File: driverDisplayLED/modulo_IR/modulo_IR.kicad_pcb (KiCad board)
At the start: 2 copper layers, 15 parts, among them J1 Conn_01x03_Male, U1 SFH617A-1X001, U2 LM393

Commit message: rediseño PCB
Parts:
- removed U1: SFH617A-1X001, Package_SO:SO-4_4.4x2.3mm_P1.27mm
- added D3: LED, LED_THT:LED_D5.0mm_Horizontal_O3.81mm_Z3.0mm, F.Cu at (111.0, 77.0)
- added D4: D_Photo, LED_THT:LED_D5.0mm_Horizontal_O3.81mm_Z3.0mm, F.Cu at (111.0, 84.5)
- C1, C2: footprint Capacitor_SMD:C_0504_1310Metric_Pad0.83x1.28mm_HandSolder -> Capacitor_SMD:C_0805_2012Metric
- D1, D2: footprint LED_THT:LED_D1.8mm_W3.3mm_H2.4mm -> Diode_SMD:D_0805_2012Metric
- J1: footprint Connector_PinHeader_2.54mm:PinHeader_1x03_P2.54mm_Vertical -> Connector_PinHeader_2.54mm:PinHeader_1x03_P2.54mm_Horizontal
- moved D2 28.2 mm to (138.9, 76.0), turned to 0 degrees
- moved D1 28.1 mm to (139.1, 88.0), turned to 0 degrees
- moved H1 5.05 mm to (137.0, 80.0)
- moved J1 3.42 mm to (144.0, 80.0)
- moved H2 1.61 mm to (115.0, 77.0)
- moved U2 1.16 mm to (129.0, 86.6)
- moved C1 0.91 mm to (121.5, 76.2), turned to 180 degrees
- moved R3 0.82 mm to (135.0, 85.9), turned to 270 degrees
- moved RV1 0.80 mm to (129.0, 78.0)
- moved R1 0.65 mm to (121.3, 88.2), turned to 180 degrees
- moved C2 0.51 mm to (121.5, 78.8), turned to 180 degrees
- moved R4 0.36 mm to (121.3, 85.8)
- moved R2 0.31 mm to (121.3, 83.5)
- moved R5 0.25 mm to (121.4, 81.2)
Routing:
- net Net-(C2-Pad1): track 41.5 -> 19.9 mm, vias 3 -> 1
- net Net-(D3-Pad2): track 13.1 -> 32.8 mm, vias 0 -> 1
- net Net-(D2-Pad1): track 11.0 -> 30.1 mm, vias 0 -> 2
- net +5V: track 104.4 -> 91.8 mm, vias 0 -> 2
- net Net-(D1-Pad1): track 10.2 -> 17.2 mm
- net Net-(RV1-Pad2): track 11.5 -> 13.6 mm
- net (no net): track 0.98 -> 0.00 mm
- net GND: vias 2 -> 0
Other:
- board outline added: 40 x 18 mm
- rule trace_min: 0.2 -> 0.3
- rule via_min_size: 0.4 -> 0.5

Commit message: rediseño PCB
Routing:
- net +5V: track 91.8 -> 93.6 mm
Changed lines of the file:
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@@
     (thickness 1.6)
     (drawings 5)
-    (tracks 95)
+    (tracks 97)
     (zones 0)
     (modules 16)
@@
   (segment (start 123.75 76.25) (end 122.5 76.25) (width 0.3) (layer F.Cu) (net 1))
   (segment (start 140 88) (end 140 87) (width 0.3) (layer F.Cu) (net 1))
-  (segment (start 138 85) (end 136 85) (width 0.3) (layer F.Cu) (net 1))
   (segment (start 140 87) (end 138 85) (width 0.3) (layer F.Cu) (net 1))
   (via (at 125 76) (size 1) (drill 0.5) (layers F.Cu B.Cu) (net 1))
@@
   (segment (start 114 82) (end 115 81) (width 0.3) (layer F.Cu) (net 1))
   (segment (start 114 84) (end 114 82) (width 0.3) (layer F.Cu) (net 1))
+  (segment (start 136.75 85) (end 135 85) (width 0.3) (layer F.Cu) (net 1))
+  (segment (start 138 85) (end 136.75 85) (width 0.3) (layer F.Cu) (net 1))
+  (segment (start 136.75 85) (end 136 85) (width 0.3) (layer F.Cu) (net 1))
   (segment (start 126.525 87.23) (end 125.23 87.23) (width 0.3) (layer F.Cu) (net 3))
   (segment (start 123.75 85.75) (end 122.25 85.75) (width 0.3) (layer F.Cu) (net 3))

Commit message: actualizo correcciones PCB, con DRC sin errores, margenes actualizdos, mounting hole y fiducial, labels, y planos de Vcc y GND
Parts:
- H2: footprint Fiducial:Fiducial_1mm_Mask2mm -> MountingHole:MountingHole_2.2mm_M2
- moved H1 22.5 mm to (115.0, 75.2)
- moved H2 21.2 mm to (136.0, 79.6)
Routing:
- net +5V: track 93.6 -> 37.6 mm, vias 2 -> 0
- net Net-(C2-Pad1): track 19.9 -> 28.1 mm, vias 1 -> 2
- net GND: track 0.00 -> 8.14 mm, vias 0 -> 2
- net Net-(D3-Pad2): track 32.8 -> 35.6 mm
- added copper zone on F.Cu, net +5V
- removed copper zone on F.Cu, net GND
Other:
- net class Default: trace_width 0.25 -> 0.3; via_dia 0.8 -> 1; via_drill 0.4 -> 0.5

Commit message: actualizo rotulo
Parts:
- moved C1 43.2 mm to (81.0, 91.2)
- moved C2 43.2 mm to (81.0, 93.8)
- moved D1 43.2 mm to (98.6, 103.0)
- moved D2 43.2 mm to (98.4, 91.0)
- moved D3 43.2 mm to (70.5, 92.0)
- moved D4 43.2 mm to (70.5, 99.5)
- moved H1 43.2 mm to (74.5, 90.2)
- moved H2 43.2 mm to (95.5, 94.6)
- moved J1 43.2 mm to (103.5, 95.0)
- moved R1 43.2 mm to (80.8, 103.2)
- moved R2 43.2 mm to (80.8, 98.5)
- moved R3 43.2 mm to (94.5, 100.9)
- moved R4 43.2 mm to (80.8, 100.8)
- moved R5 43.2 mm to (80.9, 96.2)
- moved RV1 43.2 mm to (88.5, 93.0)
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
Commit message: agrego notas de fabricacion
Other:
- board text added: "Estandar 8 mils (ref. Mayer) Grilla: 1 mm, 0.5 mm Via: 0.8 mm / 0.4 mm Margen: 0.4 mm Pista: 0.3 mm Dist a Borde: 0.5 mm Terminacion : Cu+Flux Espesor placa: 1.6 mm Espesor del Cobre: Estandar (35um/1Oz) Material: FR4"

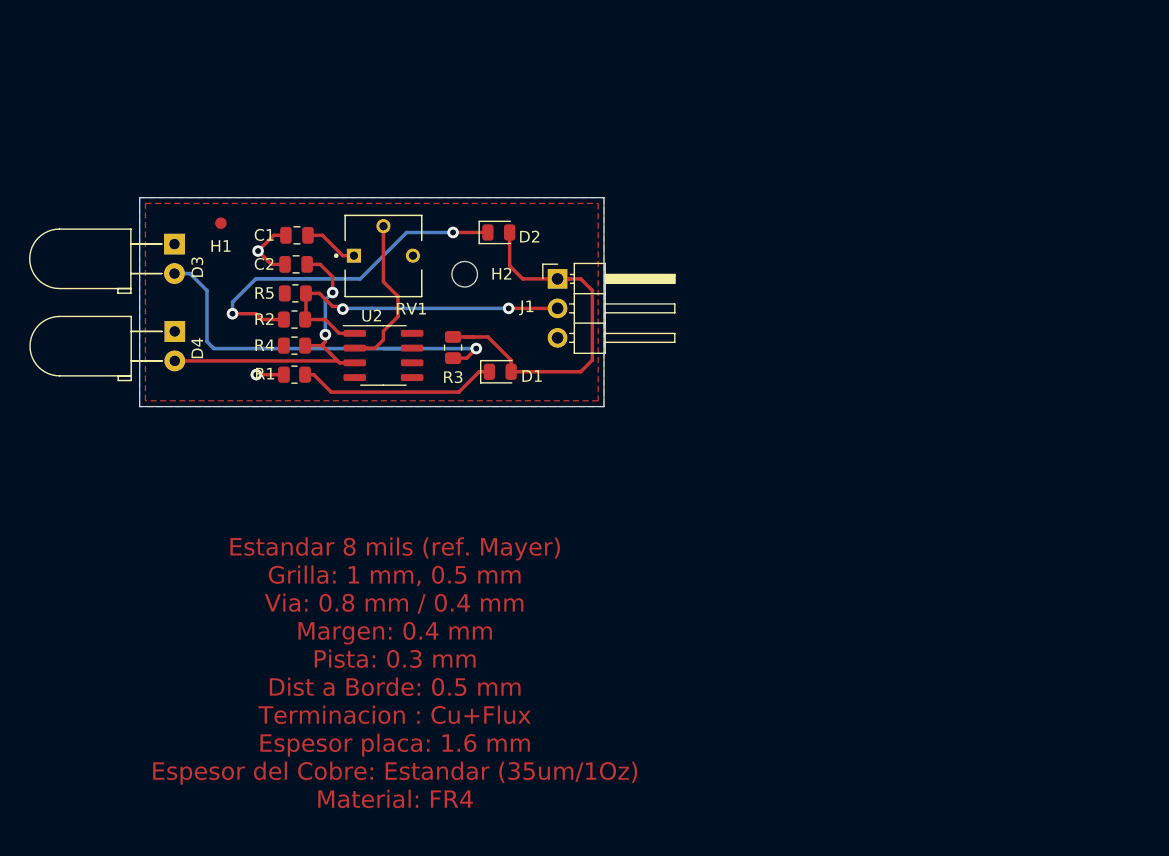
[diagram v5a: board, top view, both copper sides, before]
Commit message: agrego cotas, modelo 3d del trimmer, refill de planos
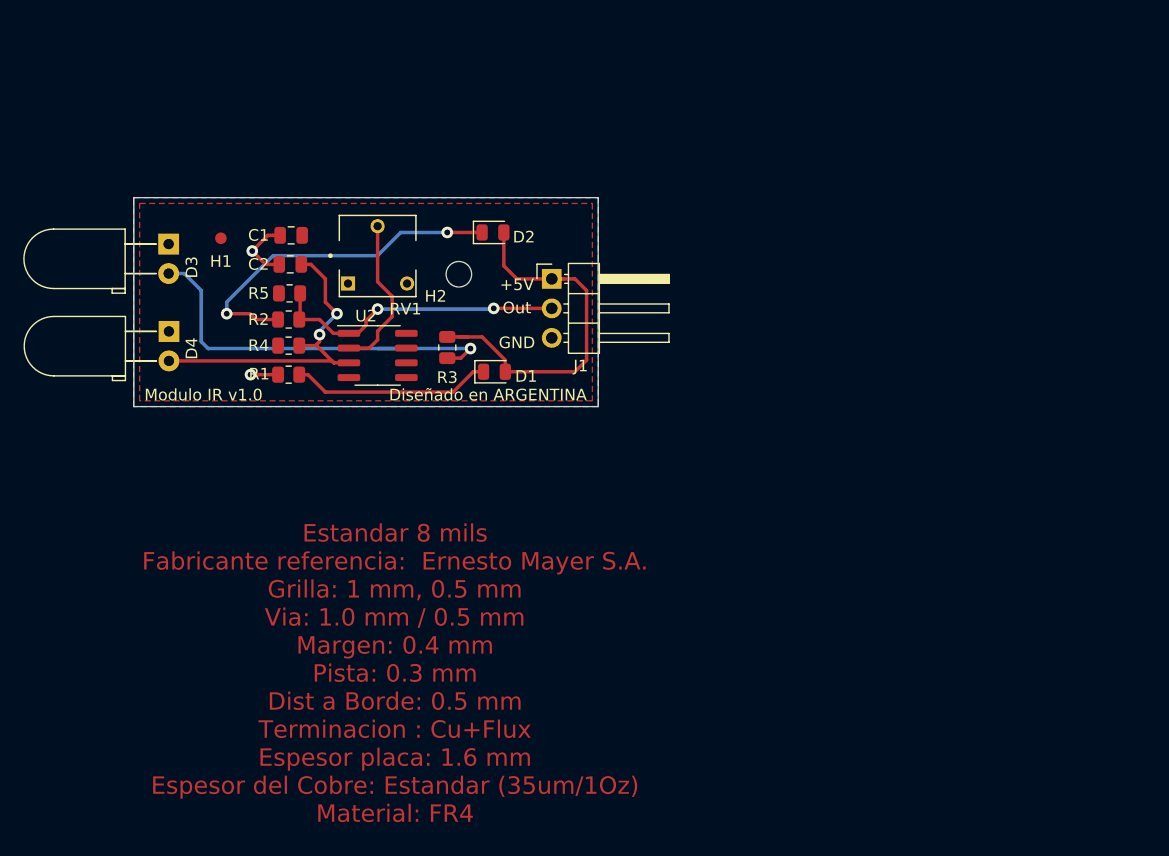
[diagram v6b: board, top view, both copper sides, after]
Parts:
- moved H1 1.30 mm to (74.5, 91.5)
- moved C1 0.50 mm to (80.5, 91.2)
- moved C2 0.50 mm to (80.5, 93.8)
- moved D1 0.50 mm to (98.1, 103.0)
- moved D2 0.50 mm to (97.9, 91.0)
- moved D3 0.50 mm to (70.0, 92.0)
- moved D4 0.50 mm to (70.0, 99.5)
- moved H2 0.50 mm to (95.0, 94.6)
- moved J1 0.50 mm to (103.0, 95.0)
- moved R1 0.50 mm to (80.3, 103.2)
- moved R2 0.50 mm to (80.3, 98.5)
- moved R3 0.50 mm to (94.0, 100.9)
- moved R4 0.50 mm to (80.3, 100.8)
- moved R5 0.50 mm to (80.4, 96.2)
- moved RV1 0.50 mm to (88.0, 93.0)
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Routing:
- net +5V: track 37.6 -> 32.9 mm
- net /D0: track 29.3 -> 25.6 mm
- net Net-(C2-Pad1): track 28.1 -> 28.6 mm
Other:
- board text added: "+5V"
- board text added: "Diseñado en ARGENTINA"
- board text added: "Estandar 8 mils Fabricante referencia: Ernesto Mayer S.A. Grilla: 1 mm, 0.5 mm Via: 1.0 mm / 0.5 mm Margen: 0.4 mm Pista: 0.3 mm Dist a Borde: 0.5 mm Terminacion : Cu+Flux Espesor placa: 1.6 mm Espesor del Cobre: Estandar (35um/1Oz) Material: FR4"
- board text added: "GND"
- board text added: "Modulo IR v1.0"
- board text added: "Out"
- board text removed: "Estandar 8 mils (ref. Mayer) Grilla: 1 mm, 0.5 mm Via: 0.8 mm / 0.4 mm Margen: 0.4 mm Pista: 0.3 mm Dist a Borde: 0.5 mm Terminacion : Cu+Flux Espesor placa: 1.6 mm Espesor del Cobre: Estandar (35um/1Oz) Material: FR4"
